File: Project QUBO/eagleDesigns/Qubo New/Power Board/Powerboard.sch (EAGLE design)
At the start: 25 parts

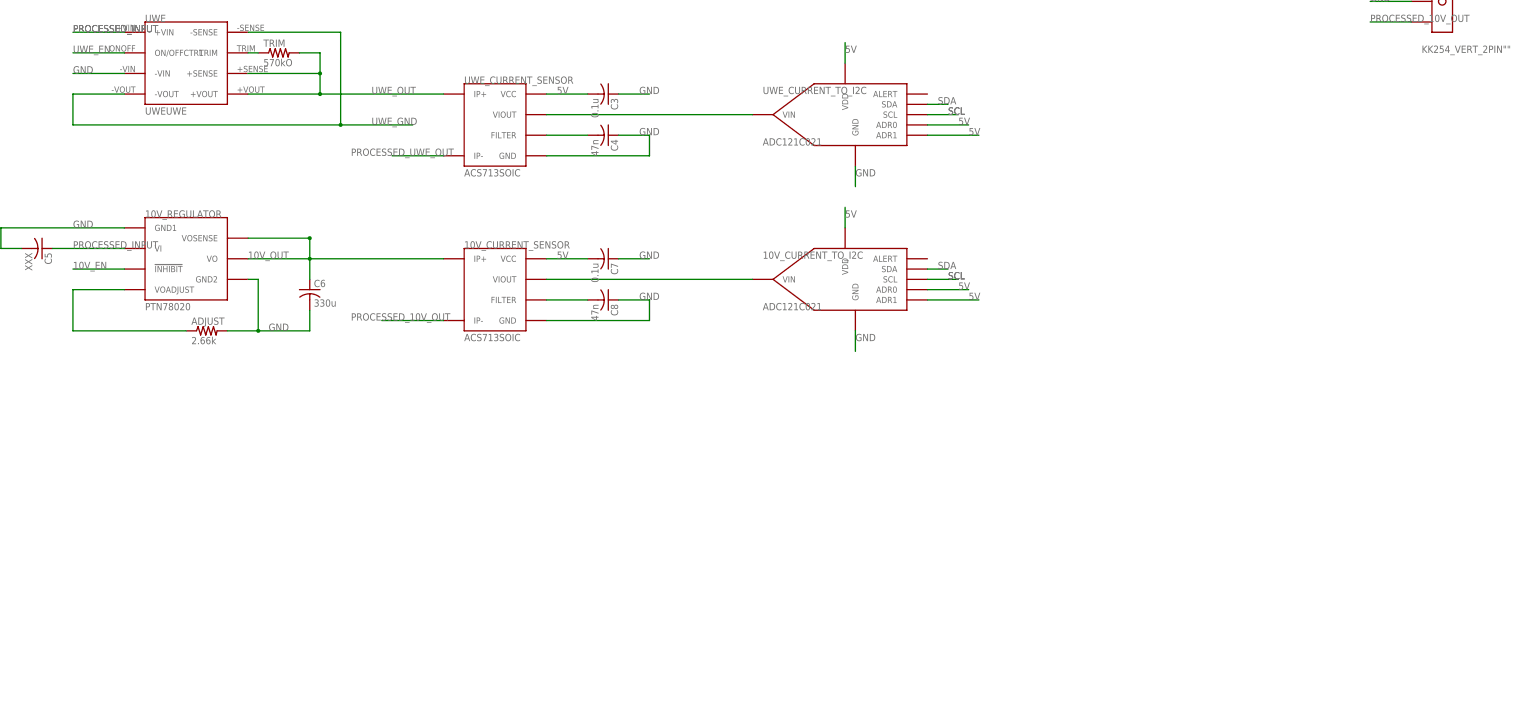
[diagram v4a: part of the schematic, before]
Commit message: 
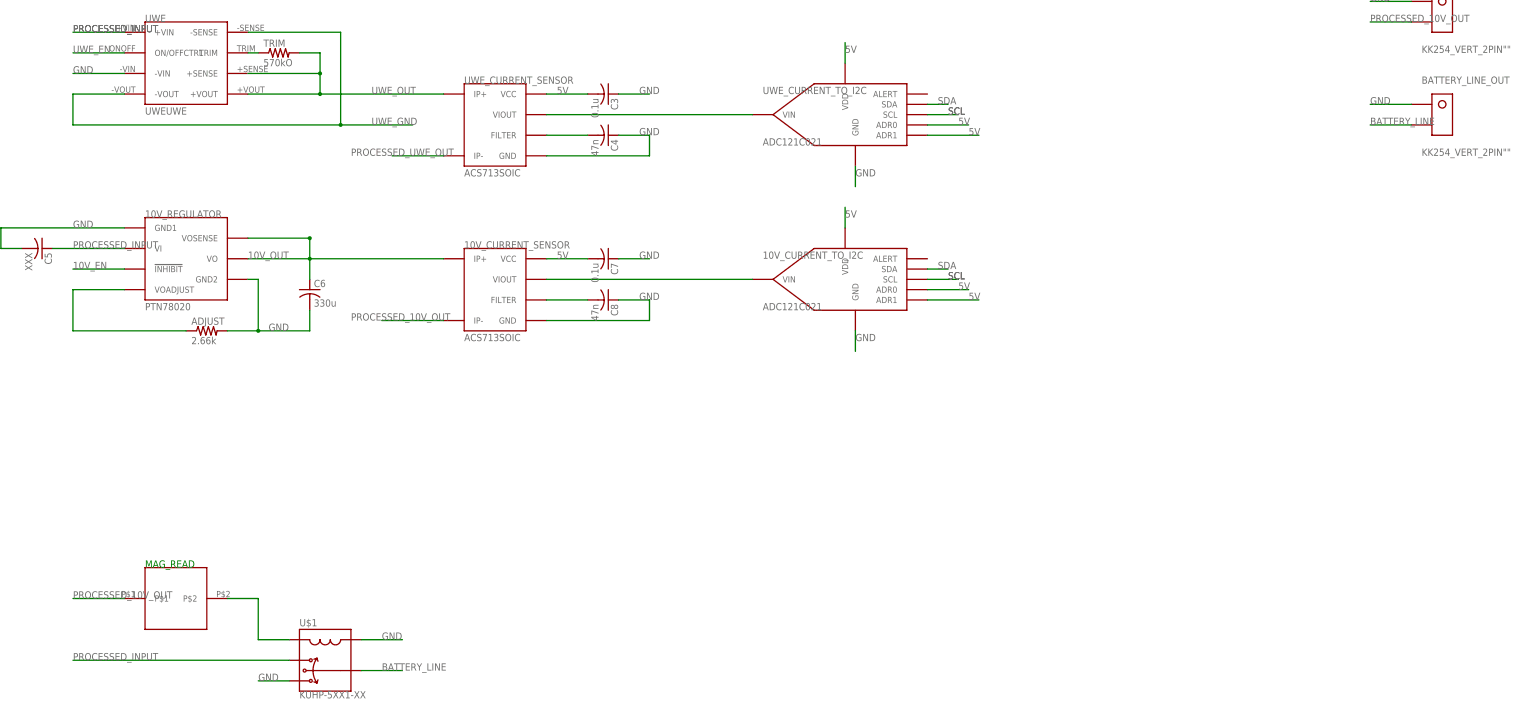
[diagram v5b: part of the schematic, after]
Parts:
- added BATTERY_LINE_OUT: KK254_VERT_2PIN"", molex:KK254_VERT_2PIN""
- added MAGREAD: HE151TR-ND, magReed:HE151TR-ND
- added U$1: KUHP-5XX1-XX, TE:KUHP-5XX1-XX
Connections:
- new net BATTERY_LINE: BATTERY_LINE_OUT.P$2, U$1.7
- new net N$9: MAGREAD.P$2, U$1.B
- net GND: now also BATTERY_LINE_OUT.P$1, U$1.5, U$1.A
- net PROCESSED_10V_OUT: now also MAGREAD.P$1
- net PROCESSED_INPUT: now also U$1.2
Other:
- note added: "MAG_READ"
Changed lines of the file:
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@@
 <part name="10V_CURRENT_TO_I2C" library="texas" deviceset="ADC121C021" device=""/>
 <part name="10V_OUT" library="molex" deviceset="KK254_VERT_2PIN" device="&quot;&quot;"/>
+<part name="MAGREAD" library="magReed" deviceset="HE151TR-ND" device=""/>
+<part name="U$1" library="TE" deviceset="KUHP-5XX1-XX" device=""/>
+<part name="BATTERY_LINE_OUT" library="molex" deviceset="KK254_VERT_2PIN" device="&quot;&quot;"/>
 </parts>
 <sheets>
 <sheet>
 <plain>
+<text x="106.68" y="-91.44" size="1.778" layer="91">MAG_READ</text>
 </plain>
 <instances>
@@
 <instance part="10V_CURRENT_TO_I2C" gate="G$1" x="279.4" y="-20.32"/>
 <instance part="10V_OUT" gate="U1" x="426.72" y="45.72"/>
+<instance part="MAGREAD" gate="G$1" x="114.3" y="-99.06"/>
+<instance part="U$1" gate="G$1" x="152.4" y="-114.3"/>
+<instance part="BATTERY_LINE_OUT" gate="U1" x="426.72" y="20.32"/>
 </instances>
 <busses>
@@
 <label x="408.94" y="48.26" size="1.778" layer="95"/>
 </segment>
+<segment>
+<pinref part="U$1" gate="G$1" pin="A"/>
+<wire x1="160.02" y1="-109.22" x2="170.18" y2="-109.22" width="0.1524" layer="91"/>
+<label x="165.1" y="-109.22" size="1.778" layer="95"/>
+</segment>
+<segment>
+<pinref part="U$1" gate="G$1" pin="5"/>
+<wire x1="142.24" y1="-119.38" x2="134.62" y2="-119.38" width="0.1524" layer="91"/>
+<label x="134.62" y="-119.38" size="1.778" layer="95"/>
+</segment>
+<segment>
+<pinref part="BATTERY_LINE_OUT" gate="U1" pin="P$1"/>
+<wire x1="419.1" y1="22.86" x2="408.94" y2="22.86" width="0.1524" layer="91"/>
+<label x="408.94" y="22.86" size="1.778" layer="95"/>
+</segment>
 </net>
 <net name="N$1" class="0">
@@
 <label x="88.9" y="-12.7" size="1.778" layer="95"/>
 <pinref part="C5" gate="G$1" pin="1"/>
+</segment>
+<segment>
+<pinref part="U$1" gate="G$1" pin="2"/>
+<wire x1="142.24" y1="-114.3" x2="88.9" y2="-114.3" width="0.1524" layer="91"/>
+<label x="88.9" y="-114.3" size="1.778" layer="95"/>
 </segment>
 </net>
@@
 <label x="408.94" y="43.18" size="1.778" layer="95"/>
 </segment>
-</net>
+<segment>
+<pinref part="MAGREAD" gate="G$1" pin="P$1"/>
+<wire x1="101.6" y1="-99.06" x2="88.9" y2="-99.06" width="0.1524" layer="91"/>
+<label x="88.9" y="-99.06" size="1.778" layer="95"/>
+</segment>
+</net>
+<net name="N$9" class="0">
+<segment>
+<pinref part="MAGREAD" gate="G$1" pin="P$2"/>
+<wire x1="127" y1="-99.06" x2="134.62" y2="-99.06" width="0.1524" layer="91"/>
+<wire x1="134.62" y1="-99.06" x2="134.62" y2="-109.22" width="0.1524" layer="91"/>
+<pinref part="U$1" gate="G$1" pin="B"/>
+<wire x1="134.62" y1="-109.22" x2="142.24" y2="-109.22" width="0.1524" layer="91"/>
+</segment>
+</net>
+<net name="BATTERY_LINE" class="0">
+<segment>
+<pinref part="U$1" gate="G$1" pin="7"/>
+<wire x1="160.02" y1="-116.84" x2="170.18" y2="-116.84" width="0.1524" layer="91"/>
+<label x="165.1" y="-116.84" size="1.778" layer="95"/>
+</segment>
+<segment>
+<pinref part="BATTERY_LINE_OUT" gate="U1" pin="P$2"/>
+<wire x1="419.1" y1="17.78" x2="408.94" y2="17.78" width="0.1524" layer="91"/>
+<label x="408.94" y="17.78" size="1.778" layer="95"/>
+</segment>
+</net>

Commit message: 
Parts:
- removed 10V_CURRENT_TO_I2C, INPUT_CURRENT_TO_I2C, INPUT_VOLTAGE_TO_I2C, UWE_CURRENT_TO_I2C: ADC121C021, texas:ADC121C021
- added 5V_CURRENT_SENSOR: ACS713SOIC, allegro:ACS713SOIC
- added 5V_OUT, I2C: KK254_VERT_2PIN"", molex:KK254_VERT_2PIN""
- added 5V_REG: LMZ120017-PIN, texas:LMZ120017-PIN
- added C10: 47n, resistor:C-USC0805
- added C9: 0.1u, resistor:C-USC0805
- added CIN1, CIN2, C_O1, C_O2, C_SS, C_SS1: (no value), capacitor-wima:C5/3.5
- added IC1: PCF8574T, texas:PCF8574T
- added OPT: BZW50, diode:BZW50
- added R_ENB, R_ENT, R_FBB, R_FBT, R_ON: (no value), resistor:R-US_R0805
- added U$2: ADS7828, texas:ADS7828
- added VDIV3: 90kO, resistor:R-US_R0805
- added VDIV4: 10kO, resistor:R-US_R0805
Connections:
- removed net N$11: 10V_CURRENT_SENSOR.VIOUT
- removed net N$7 (its old number): UWE_CURRENT_SENSOR.VIOUT
- removed net N$8: VDIV1.2, VDIV2.1
- removed net PROCESSED_UWE_OUT: UWE_CURRENT_SENSOR.IP-
- removed net UWE_OUT: TRIM.2, UWE.+SENSE, UWE.+VOUT, UWE_CURRENT_SENSOR.IP+
- new net 10V_CURRENT: 10V_CURRENT_SENSOR.VIOUT, U$2.CH3
- new net 10V_VOLTAGE: U$2.CH4, VDIV3.2, VDIV4.1
- new net 5V_CURRENT: 5V_CURRENT_SENSOR.VIOUT, U$2.CH5
- new net 5V_EN: IC1.P1, R_ENT.2
- new net INPUT_CURRENT: INPUT_CURRENT_SENSOR.VIOUT, U$2.CH0
- new net INPUT_VOLTAGE: U$2.CH1, VDIV1.2, VDIV2.1
- new net N$12: 5V_REG.RON, R_ON.1
- new net N$13: 5V_REG.SS, C_SS.2
- new net N$15: 5V_REG.VOUT, C_O1.2, C_O2.2, C_SS1.1, R_FBT.1
- new net N$16: 5V_REG.EN, OPT.C, R_ENB.1, R_ENT.1
- new net N$17: 5V_REG.FB, C_SS1.2, R_FBB.2, R_FBT.2
- new net UWE_CURRENT: U$2.CH2, UWE_CURRENT_SENSOR.VIOUT
- new net UWE_INPUT: UWE.+VIN, UWE_CURRENT_SENSOR.IP-
- net 10V_EN: now also IC1.P2
- net 5V: now also 5V_CURRENT_SENSOR.IP-, 5V_OUT.P$2, IC1.A0, IC1.VDD, U$2.REF, U$2.VDD; no longer 10V_CURRENT_TO_I2C.ADR0, 10V_CURRENT_TO_I2C.ADR1, 10V_CURRENT_TO_I2C.VDD, INPUT_CURRENT_TO_I2C.ADR0, INPUT_CURRENT_TO_I2C.ADR1, INPUT_CURRENT_TO_I2C.VDD, INPUT_VOLTAGE_TO_I2C.ADR0, INPUT_VOLTAGE_TO_I2C.ADR1, INPUT_VOLTAGE_TO_I2C.VDD, UWE_CURRENT_TO_I2C.ADR0, UWE_CURRENT_TO_I2C.ADR1, UWE_CURRENT_TO_I2C.VDD
- net GND: now also 5V_CURRENT_SENSOR.GND, 5V_OUT.P$1, C10.1, C9.1, IC1.A1, IC1.A2, IC1.VSS, U$2.A0, U$2.A1, U$2.GND, VDIV4.2; no longer 10V_CURRENT_TO_I2C.GND, 10V_OUT.P$1, INPUT_CURRENT_TO_I2C.GND, INPUT_VOLTAGE_TO_I2C.GND, UWE_CURRENT_TO_I2C.GND
- net N$3: now also 5V_CURRENT_SENSOR.FILTER, C10.2; no longer INPUT_CURRENT_SENSOR.VIOUT
- net PROCESSED_10V_OUT: now also VDIV3.1
- net PROCESSED_INPUT: now also 5V_CURRENT_SENSOR.IP+, 5V_CURRENT_SENSOR.VCC, 5V_REG.GND, 5V_REG.VIN, C9.2, CIN1.1, CIN1.2, CIN2.1, CIN2.2, C_O1.1, C_O2.1, C_SS.1, OPT.A, R_ENB.2, R_FBB.1, R_ON.2, UWE_CURRENT_SENSOR.IP+; no longer UWE.+VIN
- net PROCESSED_UWE_OUTPUT: now also TRIM.2, UWE.+SENSE, UWE.+VOUT
- net SCL: now also I2C.P$2, IC1.SCL, U$2.SCL; no longer 10V_CURRENT_TO_I2C.SCL, INPUT_CURRENT_TO_I2C.SCL, INPUT_VOLTAGE_TO_I2C.SCL, UWE_CURRENT_TO_I2C.SCL
- net SDA: now also I2C.P$1, IC1.SDA, U$2.SDA; no longer 10V_CURRENT_TO_I2C.SDA, INPUT_CURRENT_TO_I2C.SDA, INPUT_VOLTAGE_TO_I2C.SDA, UWE_CURRENT_TO_I2C.SDA
- net UWE_EN: now also IC1.P0
- net UWE_GND: now also 10V_OUT.P$1
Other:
- moved on the sheet: 10V_CURRENT_SENSOR, 10V_REGULATOR, 20A_FUSE, ADJUST, C1, C2, C3, C4, C5, C6, C7, C8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
